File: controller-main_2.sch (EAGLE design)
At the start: 18 parts

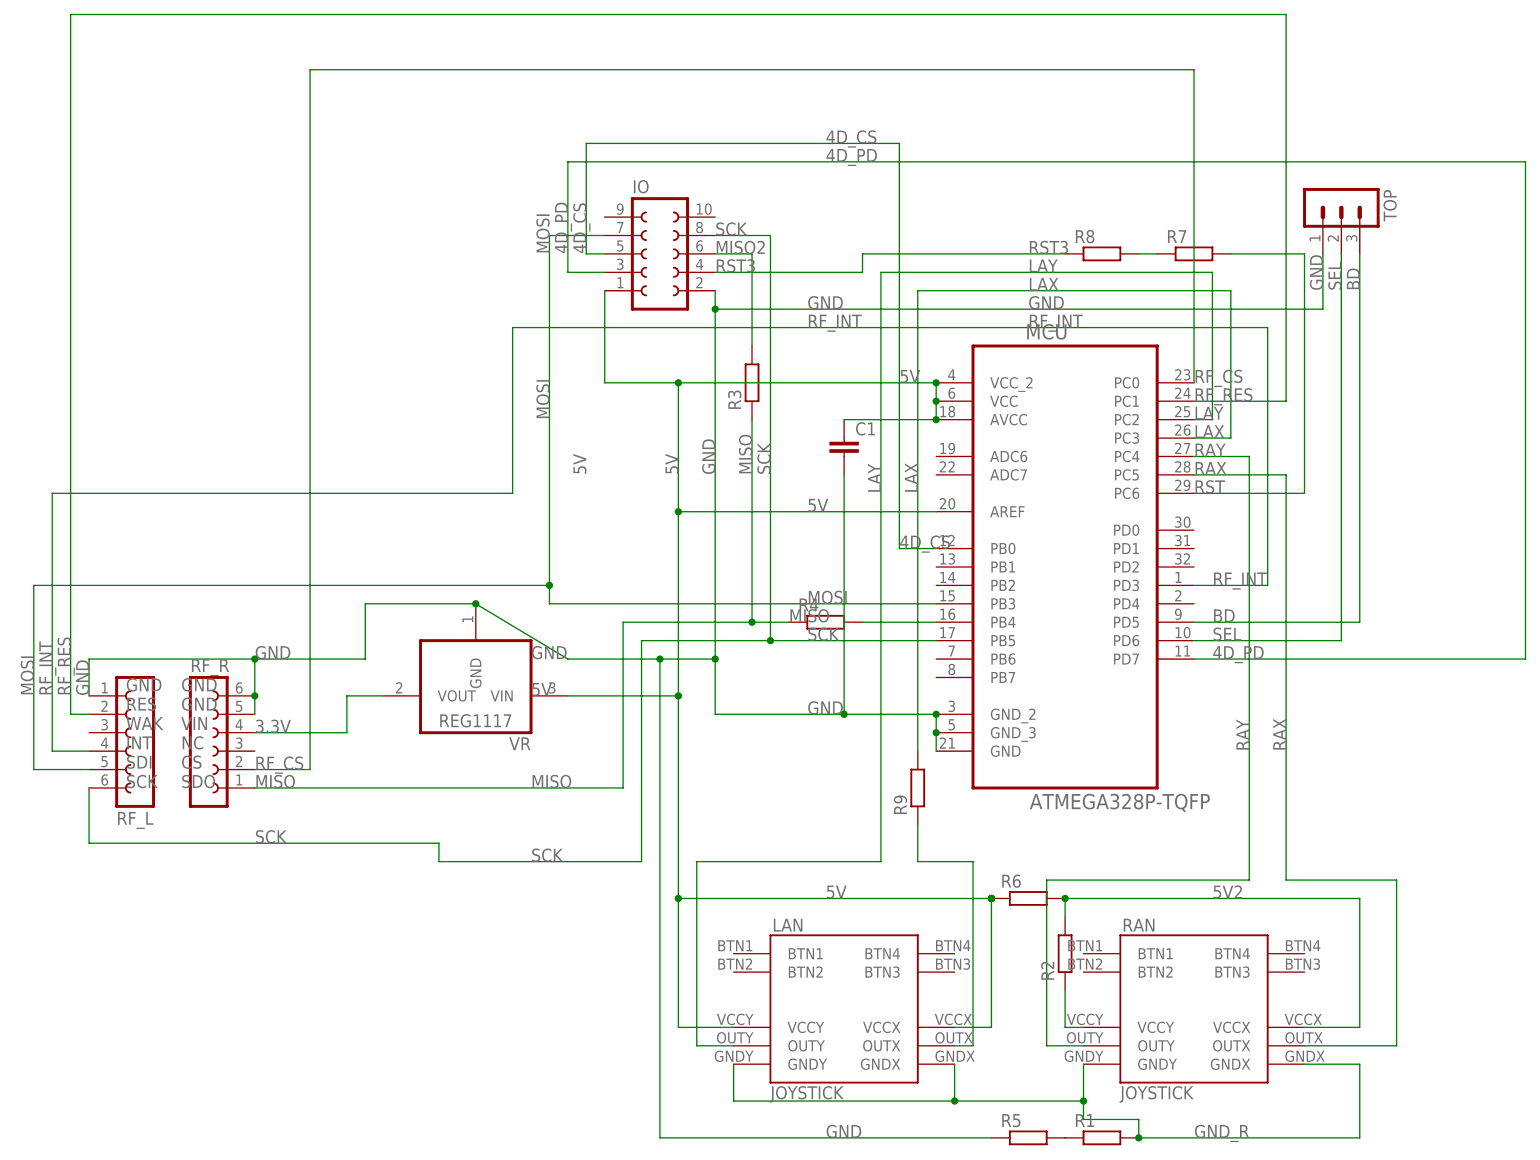
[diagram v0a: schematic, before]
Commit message: Created V2 main board, updated second board
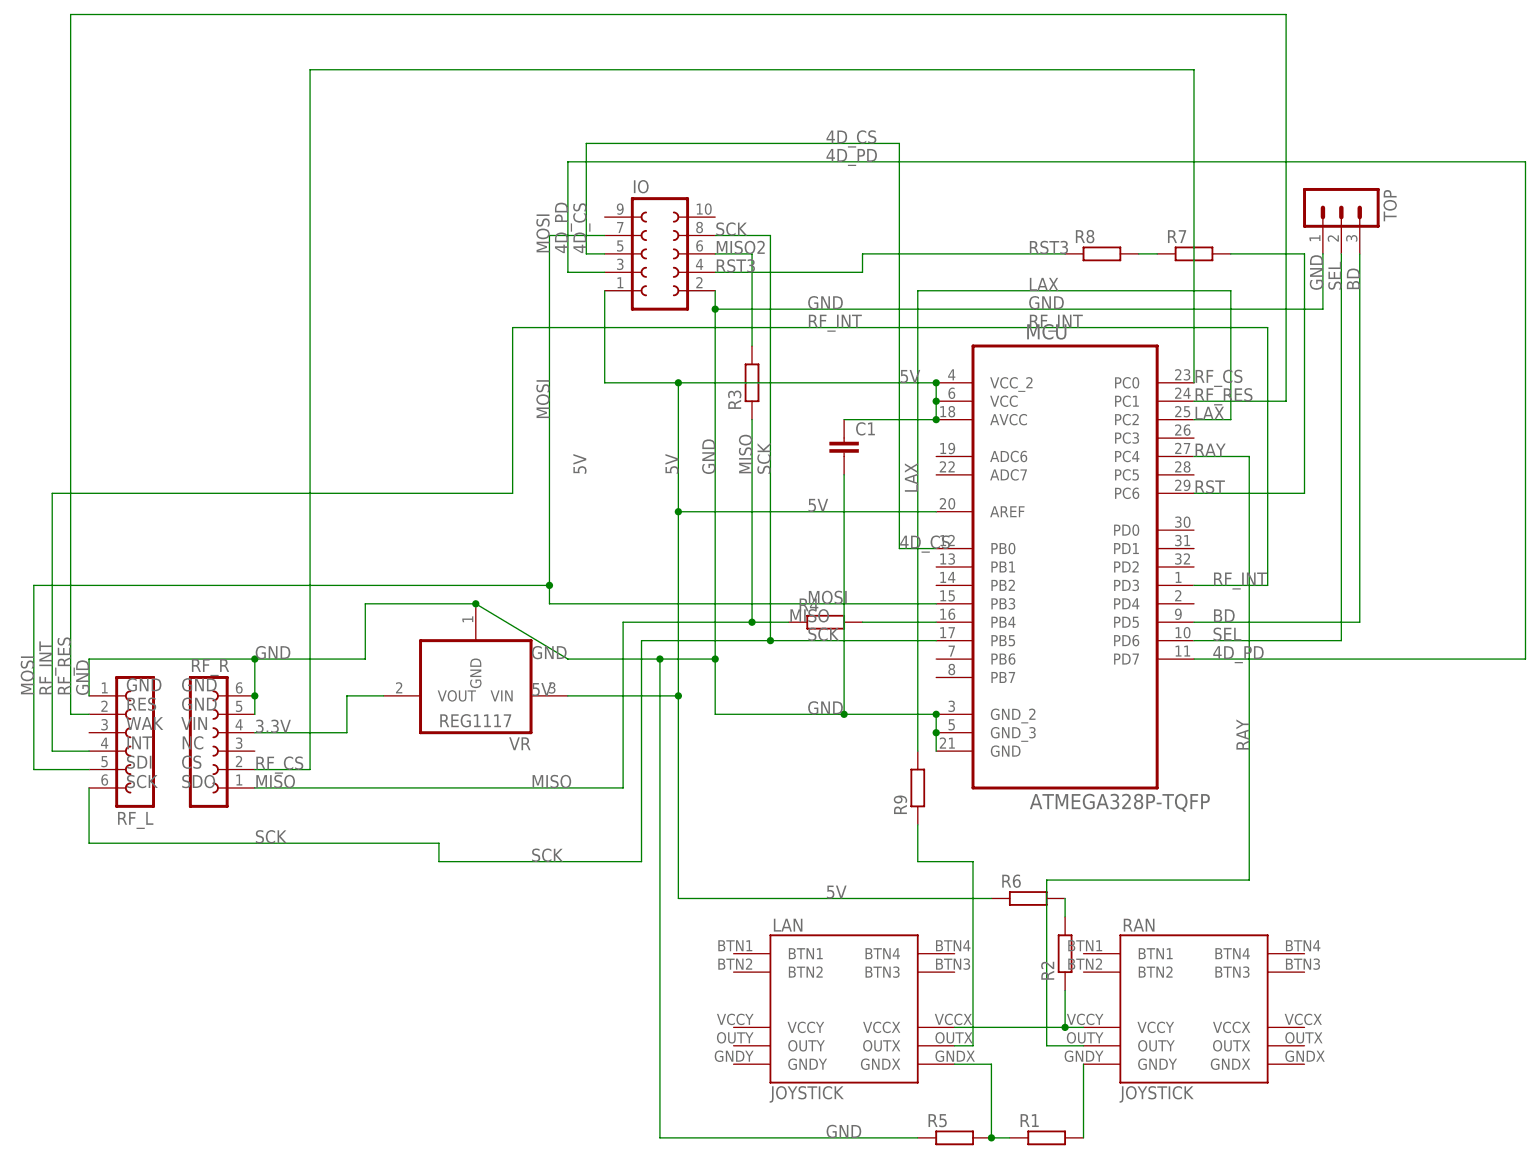
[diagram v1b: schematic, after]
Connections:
- net N$2 renamed LAX2
- removed net GND_R: LAN.GNDX, LAN.GNDY, R1.2, RAN.GNDX, RAN.GNDY
- removed net LAY: LAN.OUTY, MCU.PC2
- removed net RAX: MCU.PC5, RAN.OUTX
- new net GND2: LAN.GNDX, R1.1, R5.2
- net 5V: no longer LAN.VCCX, LAN.VCCY
- net 5V2: no longer RAN.VCCX
- net 5V_R: now also LAN.VCCX
- net LAX: now also MCU.PC2; no longer MCU.PC3
- net N$1: now also R1.2, RAN.GNDY; no longer R1.1, R5.2
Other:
- moved on the sheet: R1, R5
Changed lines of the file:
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@@
 <part name="R3" library="resistor" library_urn="urn:adsk.eagle:library:348" deviceset="R-EU_" device="M1206" package3d_urn="urn:adsk.eagle:package:26088/1"/>
 <part name="R4" library="resistor" library_urn="urn:adsk.eagle:library:348" deviceset="R-EU_" device="M1206" package3d_urn="urn:adsk.eagle:package:26088/1"/>
-<part name="R5" library="resistor" library_urn="urn:adsk.eagle:library:348" deviceset="R-EU_" device="M1206" package3d_urn="urn:adsk.eagle:package:26088/1"/>
 <part name="R6" library="resistor" library_urn="urn:adsk.eagle:library:348" deviceset="R-EU_" device="M1206" package3d_urn="urn:adsk.eagle:package:26088/1"/>
 <part name="R7" library="resistor" library_urn="urn:adsk.eagle:library:348" deviceset="R-EU_" device="M1206" package3d_urn="urn:adsk.eagle:package:26088/1"/>
 <part name="R8" library="resistor" library_urn="urn:adsk.eagle:library:348" deviceset="R-EU_" device="M1206" package3d_urn="urn:adsk.eagle:package:26088/1"/>
 <part name="R9" library="resistor" library_urn="urn:adsk.eagle:library:348" deviceset="R-EU_" device="M1206" package3d_urn="urn:adsk.eagle:package:26088/1"/>
+<part name="R5" library="resistor" library_urn="urn:adsk.eagle:library:348" deviceset="R-EU_" device="M1206" package3d_urn="urn:adsk.eagle:package:26088/1"/>
 </parts>
 <sheets>
@@
 <instance part="TOP" gate="G$1" x="175.26" y="129.54" rot="R270"/>
 <instance part="VR" gate="G$1" x="55.88" y="60.96" rot="R180"/>
-<instance part="R1" gate="G$1" x="142.24" y="0"/>
+<instance part="R1" gate="G$1" x="134.62" y="0"/>
 <instance part="R2" gate="G$1" x="137.16" y="25.4" rot="R90"/>
 <instance part="R3" gate="G$1" x="93.98" y="104.14" rot="R90"/>
 <instance part="R4" gate="G$1" x="104.14" y="71.12"/>
-<instance part="R5" gate="G$1" x="132.08" y="0"/>
 <instance part="R6" gate="G$1" x="132.08" y="33.02"/>
 <instance part="R7" gate="G$1" x="154.94" y="121.92"/>
 <instance part="R8" gate="G$1" x="142.24" y="121.92"/>
 <instance part="R9" gate="G$1" x="116.84" y="48.26" rot="R90"/>
+<instance part="R5" gate="G$1" x="121.92" y="0"/>
 </instances>
 <busses>
@@
 <wire x1="81.28" y1="66.04" x2="81.28" y2="0" width="0.1524" layer="91"/>
 <junction x="81.28" y="66.04"/>
-<wire x1="127" y1="0" x2="81.28" y2="0" width="0.1524" layer="91"/>
 <label x="88.9" y="91.44" size="1.778" layer="95" rot="R90"/>
 <label x="101.6" y="58.42" size="1.778" layer="95"/>
@@
 <pinref part="RF_R" gate="G$1" pin="6"/>
 <pinref part="RF_L" gate="G$1" pin="1"/>
+<wire x1="116.84" y1="0" x2="81.28" y2="0" width="0.1524" layer="91"/>
 <wire x1="40.64" y1="66.04" x2="40.64" y2="73.66" width="0.1524" layer="91"/>
 <wire x1="2.54" y1="60.96" x2="2.54" y2="66.04" width="0.1524" layer="91"/>
@@
 <net name="5V" class="0">
 <segment>
-<wire x1="127" y1="33.02" x2="127" y2="15.24" width="0.1524" layer="91"/>
-<pinref part="LAN" gate="G$1" pin="VCCX"/>
-<wire x1="121.92" y1="15.24" x2="127" y2="15.24" width="0.1524" layer="91"/>
 <pinref part="MCU" gate="A" pin="VCC_2"/>
 <pinref part="MCU" gate="A" pin="AVCC"/>
@@
 <pinref part="IO" gate="G$1" pin="1"/>
 <wire x1="73.66" y1="116.84" x2="73.66" y2="104.14" width="0.1524" layer="91"/>
-<pinref part="LAN" gate="G$1" pin="VCCY"/>
 <wire x1="83.82" y1="104.14" x2="83.82" y2="86.36" width="0.1524" layer="91"/>
 <wire x1="83.82" y1="86.36" x2="83.82" y2="60.96" width="0.1524" layer="91"/>
 <wire x1="83.82" y1="60.96" x2="83.82" y2="33.02" width="0.1524" layer="91"/>
-<wire x1="83.82" y1="33.02" x2="83.82" y2="15.24" width="0.1524" layer="91"/>
-<wire x1="83.82" y1="15.24" x2="91.44" y2="15.24" width="0.1524" layer="91"/>
 <junction x="83.82" y="104.14"/>
-<junction x="83.82" y="33.02"/>
 <pinref part="MCU" gate="A" pin="AREF"/>
 <wire x1="127" y1="33.02" x2="83.82" y2="33.02" width="0.1524" layer="91"/>
@@
 <junction x="119.38" y="99.06"/>
 <pinref part="VR" gate="G$1" pin="VIN"/>
-<junction x="127" y="33.02"/>
 <pinref part="R6" gate="G$1" pin="1"/>
-<junction x="127" y="33.02"/>
-</segment>
-</net>
-<net name="LAY" class="0">
-<segment>
-<wire x1="111.76" y1="119.38" x2="111.76" y2="38.1" width="0.1524" layer="91"/>
-<pinref part="LAN" gate="G$1" pin="OUTY"/>
-<wire x1="91.44" y1="12.7" x2="86.36" y2="12.7" width="0.1524" layer="91"/>
-<wire x1="86.36" y1="12.7" x2="86.36" y2="38.1" width="0.1524" layer="91"/>
-<wire x1="86.36" y1="38.1" x2="111.76" y2="38.1" width="0.1524" layer="91"/>
-<label x="111.76" y="88.9" size="1.778" layer="95" rot="R90"/>
-<wire x1="111.76" y1="119.38" x2="157.48" y2="119.38" width="0.1524" layer="91"/>
-<wire x1="157.48" y1="119.38" x2="157.48" y2="99.06" width="0.1524" layer="91"/>
-<pinref part="MCU" gate="A" pin="PC2"/>
-<wire x1="157.48" y1="99.06" x2="154.94" y2="99.06" width="0.1524" layer="91"/>
-<label x="154.94" y="99.06" size="1.778" layer="95"/>
-<label x="132.08" y="119.38" size="1.778" layer="95"/>
 </segment>
 </net>
@@
 <wire x1="116.84" y1="53.34" x2="116.84" y2="116.84" width="0.1524" layer="91"/>
 <wire x1="116.84" y1="116.84" x2="160.02" y2="116.84" width="0.1524" layer="91"/>
-<wire x1="160.02" y1="116.84" x2="160.02" y2="96.52" width="0.1524" layer="91"/>
-<pinref part="MCU" gate="A" pin="PC3"/>
-<wire x1="160.02" y1="96.52" x2="154.94" y2="96.52" width="0.1524" layer="91"/>
-<label x="154.94" y="96.52" size="1.778" layer="95"/>
+<wire x1="160.02" y1="116.84" x2="160.02" y2="99.06" width="0.1524" layer="91"/>
+<label x="154.94" y="99.06" size="1.778" layer="95"/>
 <label x="132.08" y="116.84" size="1.778" layer="95"/>
 <pinref part="R9" gate="G$1" pin="2"/>
+<pinref part="MCU" gate="A" pin="PC2"/>
+<wire x1="154.94" y1="99.06" x2="160.02" y2="99.06" width="0.1524" layer="91"/>
 </segment>
 </net>
@@
 <pinref part="MCU" gate="A" pin="PC4"/>
 <wire x1="162.56" y1="93.98" x2="154.94" y2="93.98" width="0.1524" layer="91"/>
-</segment>
-</net>
-<net name="RAX" class="0">
-<segment>
-<wire x1="167.64" y1="91.44" x2="167.64" y2="35.56" width="0.1524" layer="91"/>
-<pinref part="RAN" gate="G$1" pin="OUTX"/>
-<wire x1="167.64" y1="35.56" x2="182.88" y2="35.56" width="0.1524" layer="91"/>
-<wire x1="182.88" y1="35.56" x2="182.88" y2="12.7" width="0.1524" layer="91"/>
-<wire x1="182.88" y1="12.7" x2="170.18" y2="12.7" width="0.1524" layer="91"/>
-<label x="154.94" y="91.44" size="1.778" layer="95"/>
-<label x="167.64" y="53.34" size="1.778" layer="95" rot="R90"/>
-<pinref part="MCU" gate="A" pin="PC5"/>
-<wire x1="154.94" y1="91.44" x2="167.64" y2="91.44" width="0.1524" layer="91"/>
 </segment>
 </net>
@@
 </segment>
 </net>
-<net name="GND_R" class="0">
-<segment>
-<pinref part="RAN" gate="G$1" pin="GNDX"/>
-<wire x1="170.18" y1="10.16" x2="177.8" y2="10.16" width="0.1524" layer="91"/>
-<wire x1="177.8" y1="10.16" x2="177.8" y2="0" width="0.1524" layer="91"/>
-<wire x1="177.8" y1="0" x2="147.32" y2="0" width="0.1524" layer="91"/>
-<label x="154.94" y="0" size="1.778" layer="95"/>
-<pinref part="RAN" gate="G$1" pin="GNDY"/>
-<wire x1="139.7" y1="10.16" x2="139.7" y2="5.08" width="0.1524" layer="91"/>
-<wire x1="139.7" y1="5.08" x2="139.7" y2="2.54" width="0.1524" layer="91"/>
-<wire x1="139.7" y1="2.54" x2="147.32" y2="2.54" width="0.1524" layer="91"/>
-<wire x1="147.32" y1="2.54" x2="147.32" y2="0" width="0.1524" layer="91"/>
-<junction x="147.32" y="0"/>
-<pinref part="R1" gate="G$1" pin="2"/>
-<pinref part="LAN" gate="G$1" pin="GNDY"/>
-<wire x1="91.44" y1="10.16" x2="91.44" y2="5.08" width="0.1524" layer="91"/>
-<pinref part="LAN" gate="G$1" pin="GNDX"/>
-<wire x1="91.44" y1="5.08" x2="121.92" y2="5.08" width="0.1524" layer="91"/>
-<wire x1="121.92" y1="5.08" x2="121.92" y2="10.16" width="0.1524" layer="91"/>
-<wire x1="121.92" y1="5.08" x2="139.7" y2="5.08" width="0.1524" layer="91"/>
-<junction x="121.92" y="5.08"/>
-<junction x="139.7" y="5.08"/>
-</segment>
-</net>
 <net name="5V_R" class="0">
 <segment>
@@
 <wire x1="137.16" y1="20.32" x2="137.16" y2="15.24" width="0.1524" layer="91"/>
 <pinref part="R2" gate="G$1" pin="1"/>
+<pinref part="LAN" gate="G$1" pin="VCCX"/>
+<wire x1="121.92" y1="15.24" x2="137.16" y2="15.24" width="0.1524" layer="91"/>
+<junction x="137.16" y="15.24"/>
 </segment>
 </net>
@@
 </segment>
 </net>
-<net name="N$1" class="0">
-<segment>
-<pinref part="R1" gate="G$1" pin="1"/>
-<pinref part="R5" gate="G$1" pin="2"/>
-</segment>
-</net>
 <net name="5V2" class="0">
 <segment>
-<pinref part="RAN" gate="G$1" pin="VCCX"/>
-<wire x1="177.8" y1="15.24" x2="170.18" y2="15.24" width="0.1524" layer="91"/>
-<wire x1="177.8" y1="33.02" x2="177.8" y2="15.24" width="0.1524" layer="91"/>
-<wire x1="137.16" y1="33.02" x2="177.8" y2="33.02" width="0.1524" layer="91"/>
-<junction x="137.16" y="33.02"/>
 <pinref part="R6" gate="G$1" pin="2"/>
 <wire x1="137.16" y1="33.02" x2="137.16" y2="30.48" width="0.1524" layer="91"/>
 <pinref part="R2" gate="G$1" pin="2"/>
-<label x="157.48" y="33.02" size="1.778" layer="95"/>
 </segment>
 </net>
@@
 </segment>
 </net>
-<net name="N$2" class="0">
+<net name="LAX2" class="0">
 <segment>
 <pinref part="LAN" gate="G$1" pin="OUTX"/>
@@
 </segment>
 </net>
+<net name="N$1" class="0">
+<segment>
+<pinref part="RAN" gate="G$1" pin="GNDY"/>
+<wire x1="139.7" y1="10.16" x2="139.7" y2="0" width="0.1524" layer="91"/>
+<pinref part="R1" gate="G$1" pin="2"/>
+</segment>
+</net>
+<net name="GND2" class="0">
+<segment>
+<pinref part="LAN" gate="G$1" pin="GNDX"/>
+<wire x1="127" y1="10.16" x2="121.92" y2="10.16" width="0.1524" layer="91"/>
+<pinref part="R1" gate="G$1" pin="1"/>
+<pinref part="R5" gate="G$1" pin="2"/>
+<wire x1="127" y1="0" x2="129.54" y2="0" width="0.1524" layer="91"/>
+<wire x1="127" y1="10.16" x2="127" y2="0" width="0.1524" layer="91"/>
+<junction x="127" y="0"/>
+</segment>
+</net>
